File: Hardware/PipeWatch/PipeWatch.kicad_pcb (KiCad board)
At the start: 2 copper layers, 100.2 x 100.1 mm, 20 parts, among them J1 WJ126V-5.0-2P, J2 Conn_01x04_Pin, J3 UART, J4 JTAG, U1 IRM-10-5_C20618064, U3 ESP32-S3-WROOM-1-N16R8, U5 XIAO-ESP32-S3-DIP

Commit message: tweeked the Layout
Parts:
- added C5: 10n, Capacitor_SMD:C_0603_1608Metric, F.Cu at (100.7, 68.0)
- added R10: R_Photo, OptoDevice:R_LDR_5.0x4.1mm_P3mm_Vertical, F.Cu at (102.0, 73.5)
- added R11: 10M, Resistor_SMD:R_0603_1608Metric, F.Cu at (100.7, 70.0)
- J2: value Conn_01x04_Pin -> A02YYUW
- moved U2 48.6 mm to (99.8, 137.4)
- moved R1 46.1 mm to (113.0, 142.4)
- moved R2 46.1 mm to (109.0, 142.4)
- moved J1 33.6 mm to (169.0, 129.5), turned to -90 degrees
- moved U1 25.7 mm to (140.0, 133.1)
- moved J2 22.0 mm to (131.5, 120.0), turned to 90 degrees
- moved J4 16.6 mm to (106.2, 89.0)
- moved J3 16.3 mm to (99.7, 89.0)
- moved U5 15.0 mm to (125.0, 62.3)
- moved S1 13.9 mm to (98.0, 127.6), turned to 90 degrees
- moved S2 12.3 mm to (107.8, 127.6), turned to 90 degrees
- moved C1 11.7 mm to (100.3, 129.9)
- moved R7 7.88 mm to (120.2, 113.3)
- moved C2 7.88 mm to (98.3, 118.5)
- moved C3 7.88 mm to (98.3, 120.5)
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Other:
- board size 100.2 x 100.1 mm -> 96.5 x 100 mm
- board text added: "JLCJLCJLCJLC"
- board text added: "RST BOOT"

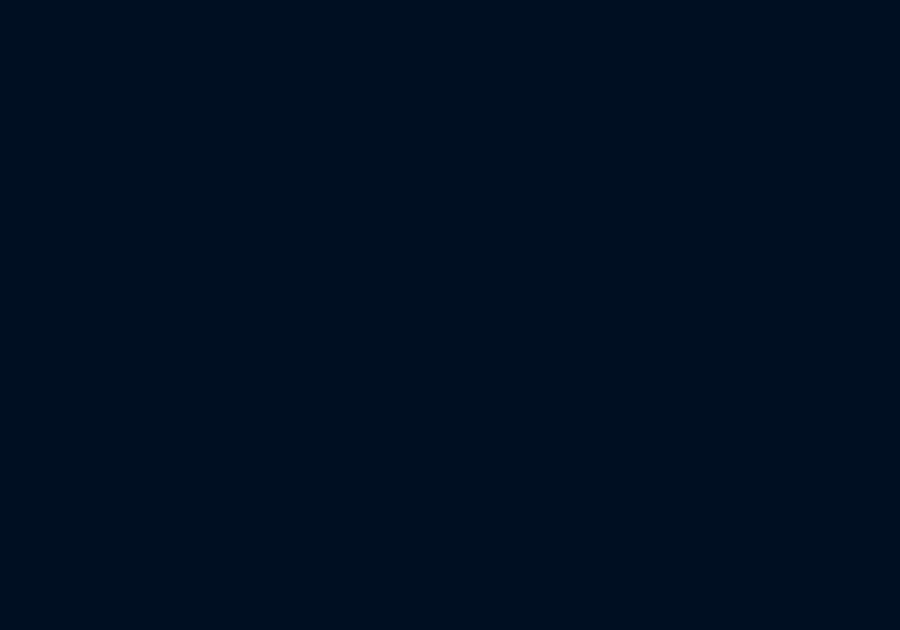
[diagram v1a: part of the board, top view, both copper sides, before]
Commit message: Started implementing the accelerometer
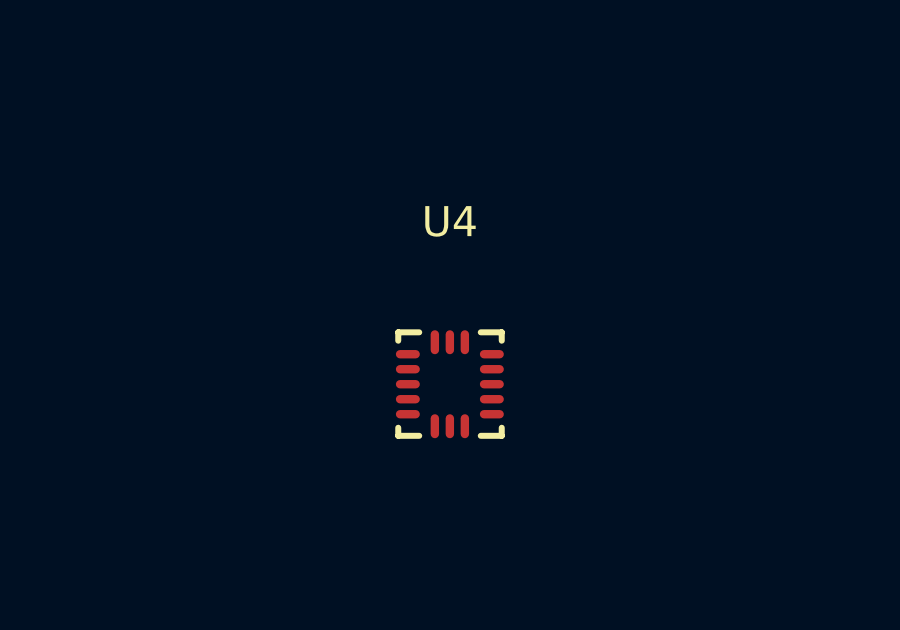
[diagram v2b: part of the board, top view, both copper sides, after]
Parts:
- added U4: LIS3DHTR_C15134, EasyEDA:LGA-16_L3.0-W3.0-P0.50-TL, F.Cu at (164.6, 91.0)

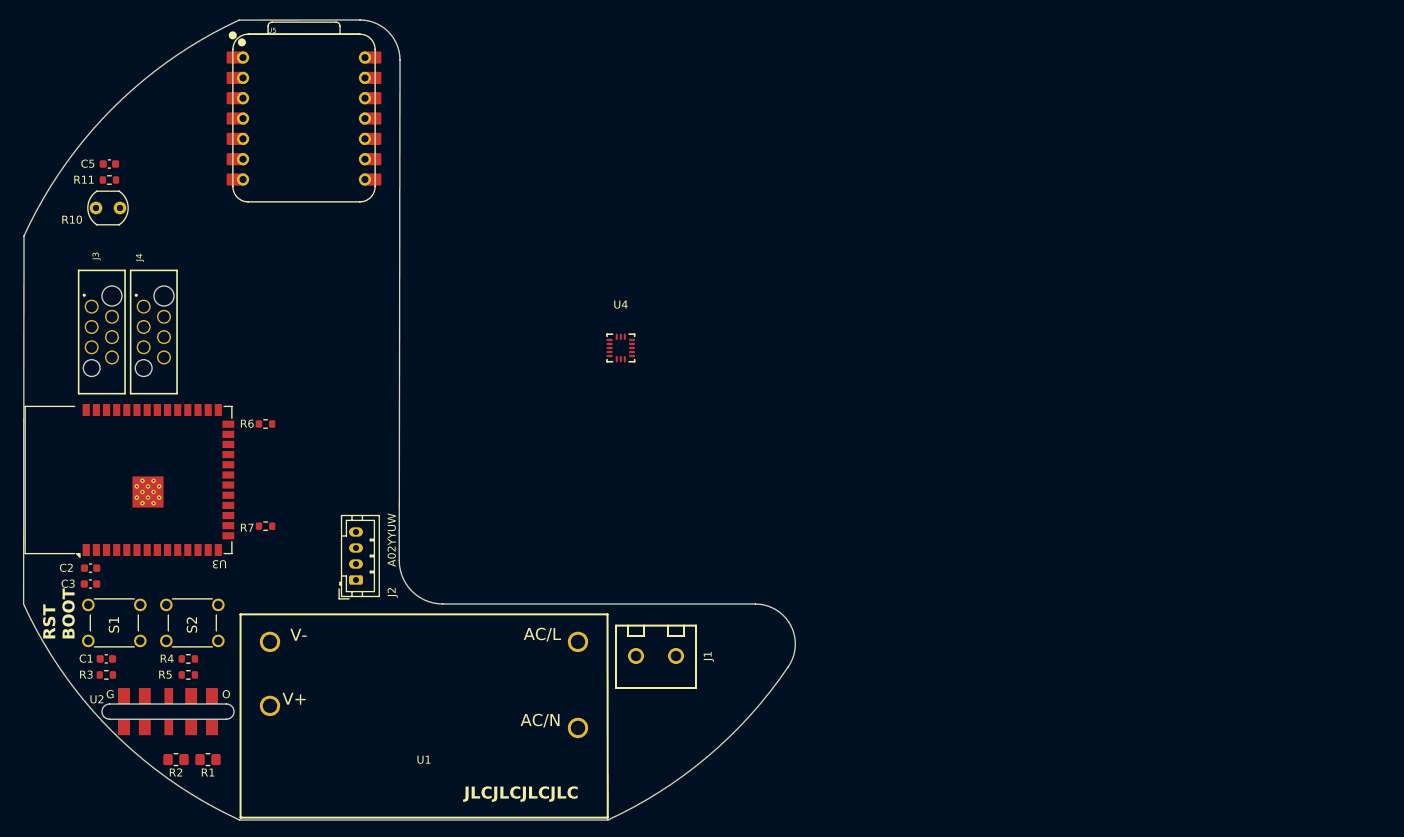
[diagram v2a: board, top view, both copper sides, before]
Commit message: added Binky parts and a load of 3d references
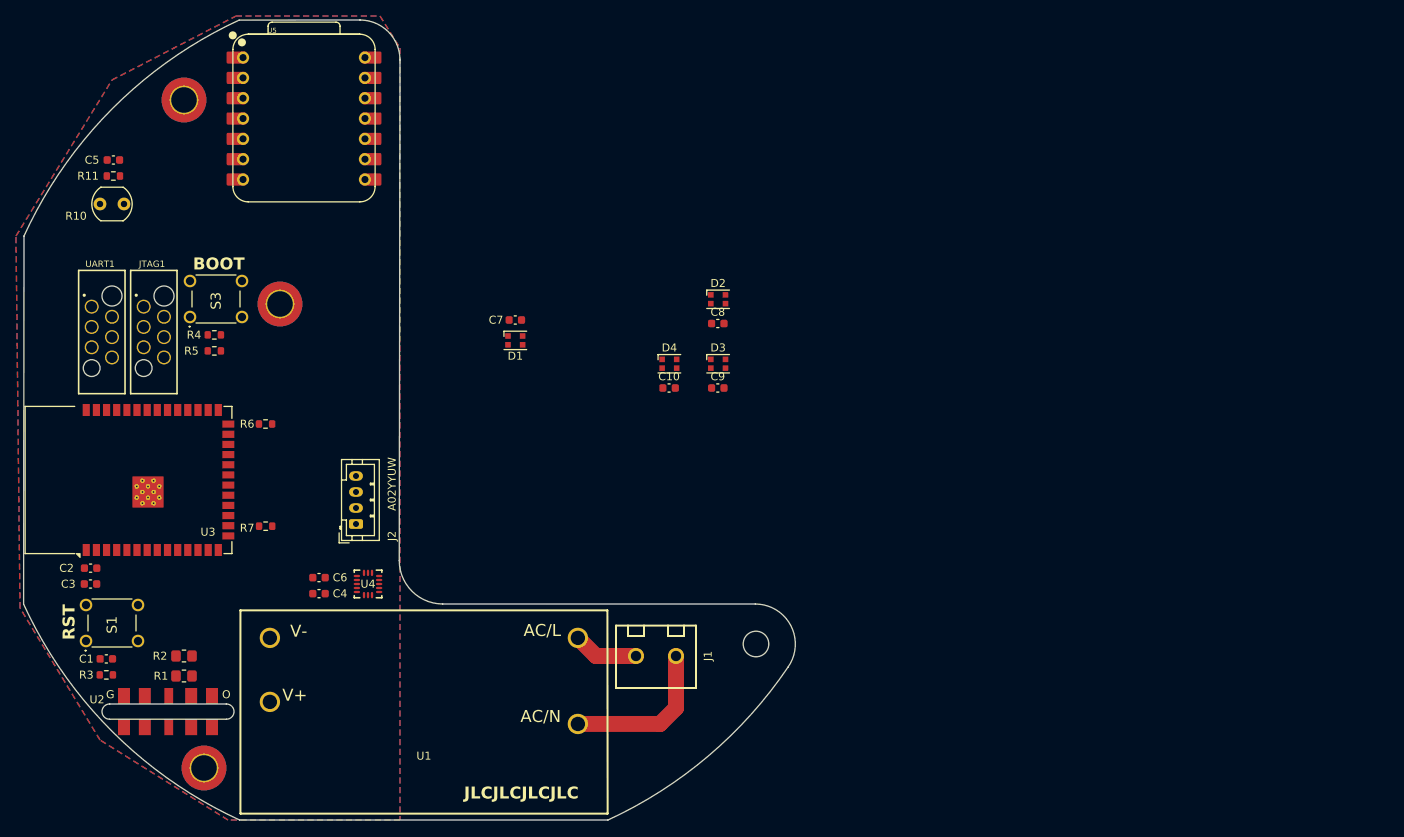
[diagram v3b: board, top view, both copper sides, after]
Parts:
- removed J3: UART, Felix_ProgHeader:490107670612
- removed J4: JTAG, Felix_ProgHeader:490107670612
- removed S2: TL1105AF160Q, Library:TL1105AF160Q
- added C10: 100n, Capacitor_SMD:C_0603_1608Metric, F.Cu at (170.6, 96.0)
- added C4: 100n, Capacitor_SMD:C_0603_1608Metric, F.Cu at (126.9, 121.7)
- added C6: 10u, Capacitor_SMD:C_0603_1608Metric, F.Cu at (126.9, 119.7)
- added C7: 100n, Capacitor_SMD:C_0603_1608Metric, F.Cu at (151.4, 87.5)
- added C8: 100n, Capacitor_SMD:C_0603_1608Metric, F.Cu at (176.7, 87.9)
- added C9: 100n, Capacitor_SMD:C_0603_1608Metric, F.Cu at (176.7, 96.0)
- added D1: WS2812B-2020, Felix:LED_WS2812B-2020_PLCC4_2.0x2.0mm, F.Cu at (151.4, 90.0)
- added D2: WS2812B-2020, Felix:LED_WS2812B-2020_PLCC4_2.0x2.0mm, F.Cu at (176.8, 84.9)
- added D3: WS2812B-2020, Felix:LED_WS2812B-2020_PLCC4_2.0x2.0mm, F.Cu at (176.8, 93.0)
- added D4: WS2812B-2020, Felix:LED_WS2812B-2020_PLCC4_2.0x2.0mm, F.Cu at (170.7, 93.0)
- added H1: MountingHole, MountingHole:MountingHole_3.2mm_M3, F.Cu at (181.5, 128.0)
- added H2: MountingHole_Pad, MountingHole:MountingHole_3.2mm_M3_DIN965_Pad_TopBottom, F.Cu at (110.0, 60.0)
- added H3: MountingHole_Pad, MountingHole:MountingHole_3.2mm_M3_DIN965_Pad_TopBottom, F.Cu at (122.0, 85.5)
- added H4: MountingHole_Pad, MountingHole:MountingHole_3.2mm_M3_DIN965_Pad_TopBottom, F.Cu at (112.5, 143.5)
- added JTAG1: 490107670612, Felix_Connectors:490107670612, F.Cu at (106.2, 89.0)
- added S3: TL1105AF160Q, Felix:TL1105AF160Q, F.Cu at (110.8, 87.1)
- added UART1: 490107670612, Felix_Connectors:490107670612, F.Cu at (99.7, 89.0)
- J1: footprint Felix:CONN-TH_WJ126V-5.0-2P -> Felix_Connectors:CONN-TH_WJ126V-5.0-2P
- S1: footprint Library:TL1105AF160Q -> Felix:TL1105AF160Q
- moved U4 43.2 mm to (133.0, 120.5)
- moved R4 40.6 mm to (113.8, 89.4), turned to 180 degrees
- moved R5 40.6 mm to (113.8, 91.4)
- moved R2 13.0 mm to (110.0, 129.5), turned to 0 degrees
- moved R1 10.9 mm to (110.0, 132.0)
- moved J2 7.00 mm to (131.5, 113.0)
- moved C5 0.71 mm to (101.2, 67.5)
- moved R10 0.71 mm to (102.5, 73.0)
- moved R11 0.71 mm to (101.2, 69.5)
- moved U1 0.50 mm to (140.0, 132.6)
- moved S1 0.29 mm to (97.8, 127.6)
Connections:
- U4 pad 1: unconnected-(U4-VDD_IO-Pad1) -> +3.3V
- U4 pad 10: unconnected-(U4-RES-Pad10) -> GND
- U4 pad 11: unconnected-(U4-INT1-Pad11) -> /MSU/INT1
- U4 pad 12: unconnected-(U4-GND-Pad12) -> GND
- U4 pad 14: unconnected-(U4-VDD-Pad14) -> +3.3V
- U4 pad 4: unconnected-(U4-SCL/SPC-Pad4) -> /MSU/SPC
- U4 pad 5: unconnected-(U4-GND-Pad5) -> GND
- U4 pad 6: unconnected-(U4-SDA/SDI/SDO-Pad6) -> /MSU/SDI
- U4 pad 7: unconnected-(U4-SDO/SA0-Pad7) -> /MSU/SAO
- U4 pad 8: unconnected-(U4-CS-Pad8) -> /MSU/CS
- U4 pad 9: unconnected-(U4-INT2-Pad9) -> /MSU/INT2
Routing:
- net Net-(J1-Pin_1): track 0.00 -> 19.6 mm
- net Net-(J1-Pin_2): track 0.00 -> 8.20 mm
- added copper zone on B.Cu, net GND
- added copper zone on F.Cu, net GND
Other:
- board text added: "BOOT"
- board text added: "RST"
- board text removed: "RST BOOT"

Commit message: some changes
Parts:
- added C11: 100n, Capacitor_SMD:C_0603_1608Metric, F.Cu at (157.2, 70.5)
- added J3: Taster, Connector_PinHeader_2.54mm:PinHeader_1x02_P2.54mm_Vertical, F.Cu at (157.5, 64.4)
- added J4: TasterLED, Connector_PinHeader_2.54mm:PinHeader_1x02_P2.54mm_Vertical, F.Cu at (162.0, 64.0)
- added R8: 10k, Resistor_SMD:R_0603_1608Metric, F.Cu at (157.2, 73.0)
- C6: footprint Capacitor_SMD:C_0603_1608Metric -> Capacitor_SMD:CP_Elec_4x5.8
- J2: footprint Connector_JST:JST_PH_B4B-PH-K_1x04_P2.00mm_Vertical -> Connector_JST:JST_XH_B4B-XH-A_1x04_P2.50mm_Vertical
- moved D2 17.4 mm to (160.4, 91.0)
- moved C8 16.3 mm to (160.4, 88.4)
- moved C9 14.4 mm to (164.5, 88.4)
- moved D3 12.4 mm to (164.5, 91.0)
- moved C10 7.89 mm to (168.5, 88.4)
- moved C7 5.25 mm to (156.6, 88.4)
- moved D1 5.25 mm to (156.6, 91.0)
- moved D4 2.97 mm to (168.5, 91.0)
- moved C6 1.21 mm to (126.7, 118.5), turned to 0 degrees
- moved J2 1.00 mm to (131.5, 112.0)
- moved C4 0.33 mm to (126.7, 122.0), turned to 0 degrees

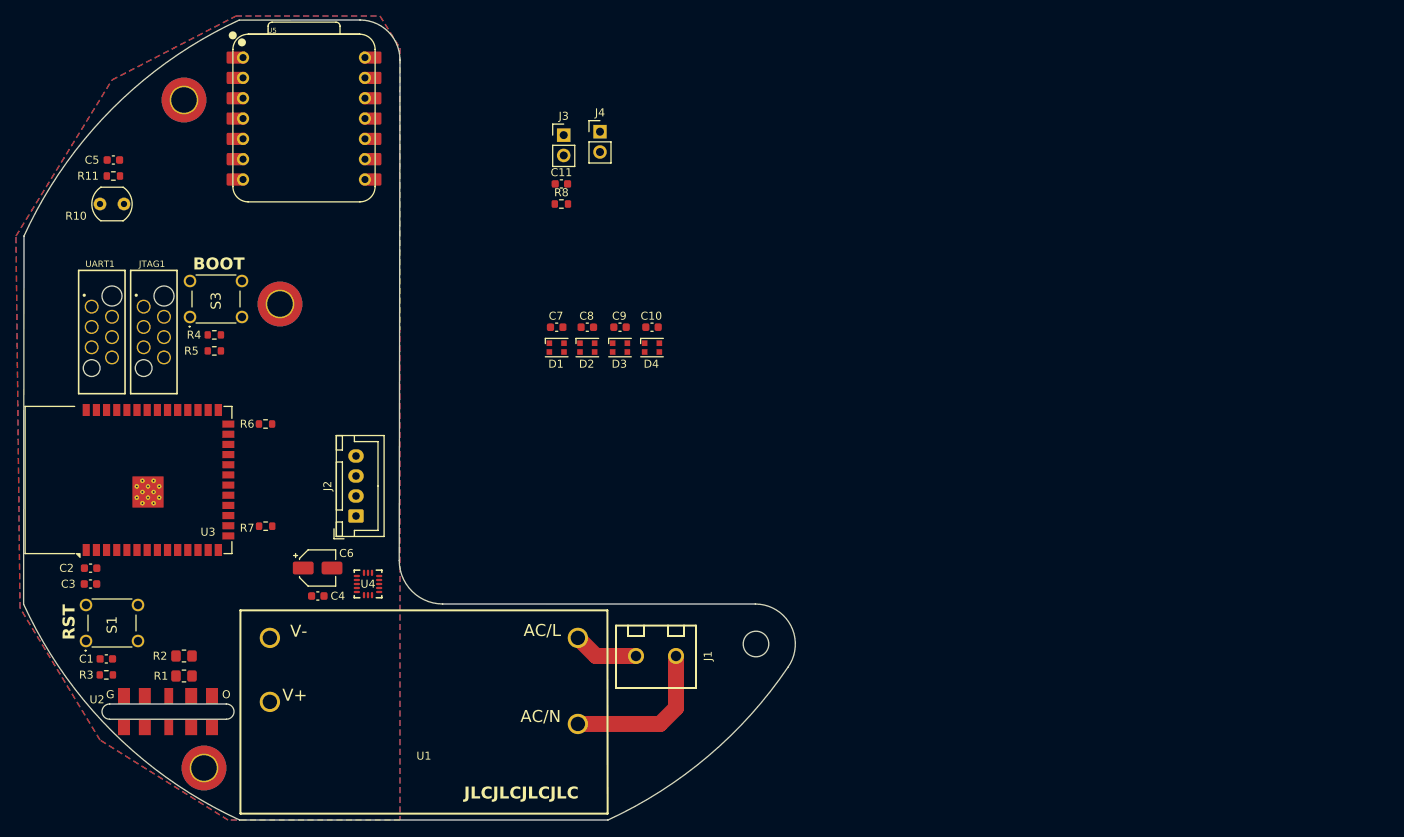
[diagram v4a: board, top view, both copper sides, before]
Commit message: Added Ten Sensor
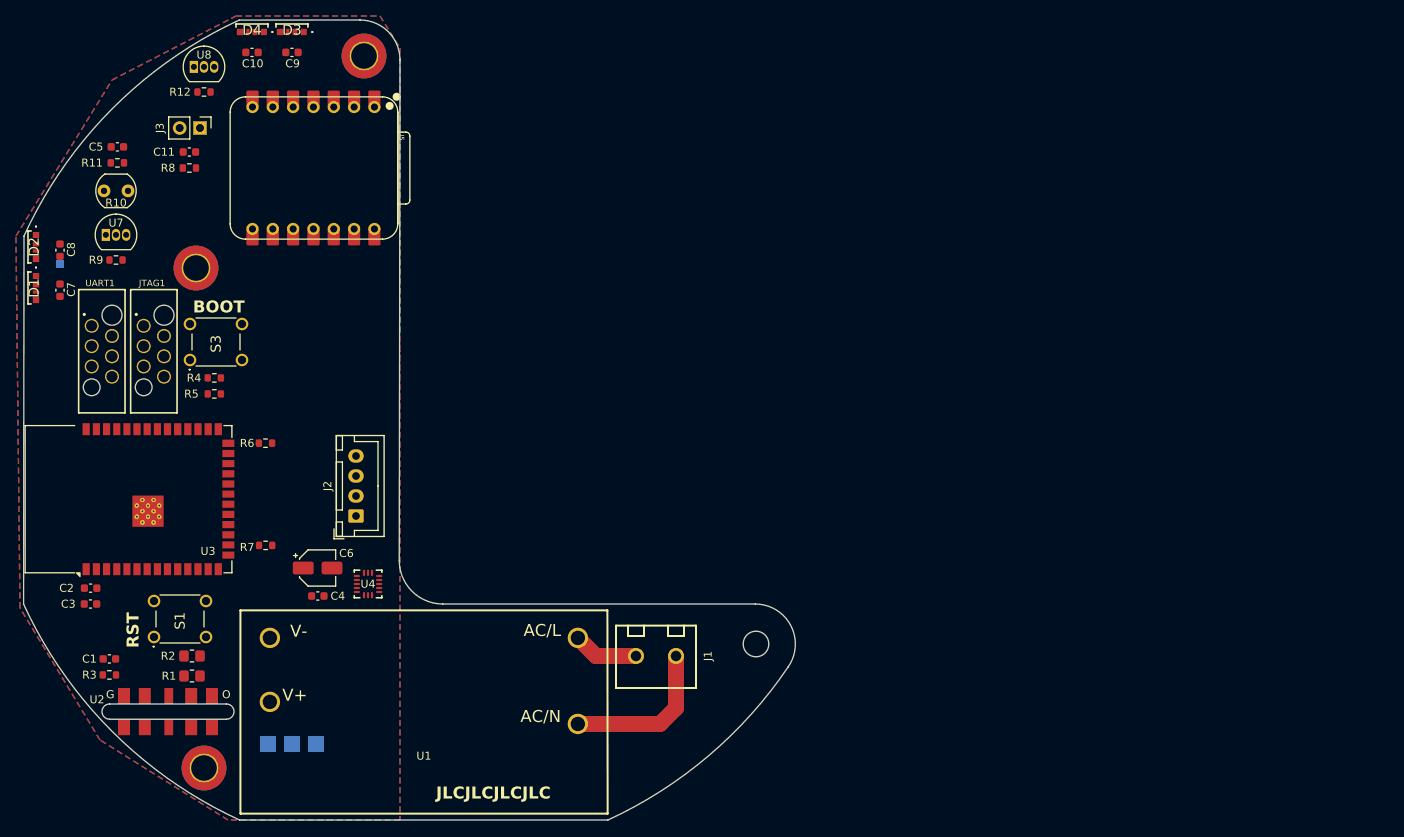
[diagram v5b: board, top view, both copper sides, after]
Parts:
- removed J4: TasterLED, Connector_PinHeader_2.54mm:PinHeader_1x02_P2.54mm_Vertical
- added R12: 4k7, Resistor_SMD:R_0603_1608Metric, F.Cu at (112.5, 59.0)
- added R9: 4k7, Resistor_SMD:R_0603_1608Metric, F.Cu at (101.5, 80.0)
- added TP1: Neopixel, TestPoint:TestPoint_Pad_1.0x1.0mm, B.Cu at (94.5, 80.5)
- added TP2: 3V3, TestPoint:TestPoint_Pad_2.0x2.0mm, B.Cu at (120.5, 140.5)
- added TP3: 5V, TestPoint:TestPoint_Pad_2.0x2.0mm, B.Cu at (123.5, 140.5)
- added TP5: GND, TestPoint:TestPoint_Pad_2.0x2.0mm, B.Cu at (126.5, 140.5)
- added U7: DS18B20, Package_TO_SOT_THT:TO-92_Inline, F.Cu at (100.2, 76.9)
- added U8: DS18B20, Package_TO_SOT_THT:TO-92_Inline, F.Cu at (111.2, 55.9)
- D1, D2, D3, D4: footprint Felix:LED_WS2812B-2020_PLCC4_2.0x2.0mm -> Felix:LED_4691_Neopixel_Edge
- moved D2 70.1 mm to (91.5, 78.4), turned to -90 degrees
- moved C8 66.6 mm to (94.5, 78.8), turned to -90 degrees
- moved D1 65.5 mm to (91.5, 83.5), turned to -90 degrees
- moved D4 63.7 mm to (118.5, 51.5), turned to 180 degrees
- moved C7 62.3 mm to (94.5, 83.8), turned to -90 degrees
- moved C10 60.7 mm to (118.5, 54.0), turned to 180 degrees
- moved D3 56.9 mm to (123.5, 51.5), turned to 180 degrees
- moved C9 53.5 mm to (123.5, 54.0), turned to 180 degrees
- moved R8 46.7 mm to (110.7, 68.5)
- moved C11 46.7 mm to (110.7, 66.5), turned to 180 degrees
- moved J3 45.5 mm to (112.0, 63.5), turned to -90 degrees
- moved H2 23.2 mm to (132.5, 54.5)
- moved H3 11.4 mm to (111.5, 81.0)
- moved S1 8.51 mm to (106.2, 127.1)
- moved U5 6.29 mm to (126.2, 68.5), turned to -90 degrees
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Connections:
- net /Taster/OUT renamed /TasterCall/OUT

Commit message: added adc
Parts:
- added U6: ADS1115IDGS, Package_SO:VSSOP-10_3x3mm_P0.5mm, F.Cu at (146.3, 85.3)
